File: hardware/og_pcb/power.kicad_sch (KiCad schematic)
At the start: 6 parts, among them J1 USB_C_Receptacle_PowerOnly_6P, U4 BD33FC0FP

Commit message: updated pcb work in progress (incomplete)
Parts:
- removed J1: USB_C_Receptacle_PowerOnly_6P, Connector_USB:USB_C_Receptacle_HRO_TYPE-C-31-M-17, symbol Connector:USB_C_Receptacle_PowerOnly_6P
- removed R8, R9: 5.1k, Resistor_SMD:R_0402_1005Metric, symbol Device:R
- added J3: Barrel_Jack, symbol Connector:Barrel_Jack
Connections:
- net GND: now also J3.2
- net VBUS: now also J3.1
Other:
- note added: "replace usbc power with barrel jack"
- note removed: "(5V Input)"
- note removed: "USB-C Power Input"

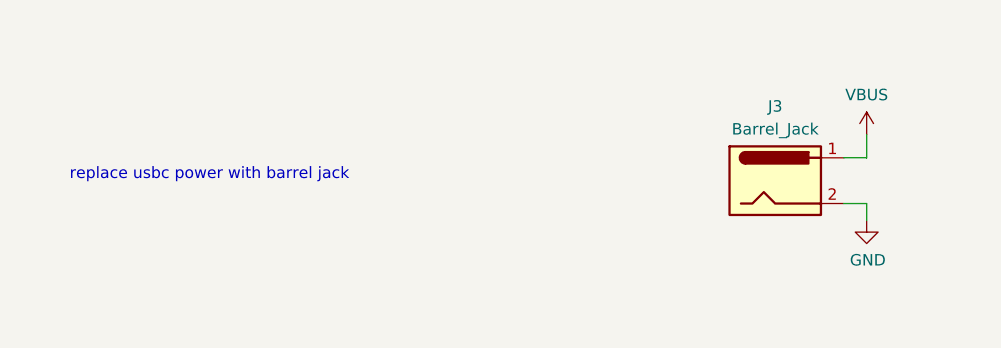
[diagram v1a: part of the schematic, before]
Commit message: updated pcb v2 progress
reimplemented spi microSD, changed power monitor to model with internal shunt resistor, changed power supply from usbc to barrel jack, reconnected vbus to microusb, modified spi and i2c connections (2 i2c connections, 2 spi connections), removed RF module & IMU.

to do:
- find/create footprints for new parts
- verify implementation by reviewing datasheets again
- implement coax connector for analog connection to cosmic watch
- implement gps receiver (must do more research; implement one well-known/documented/used b4)
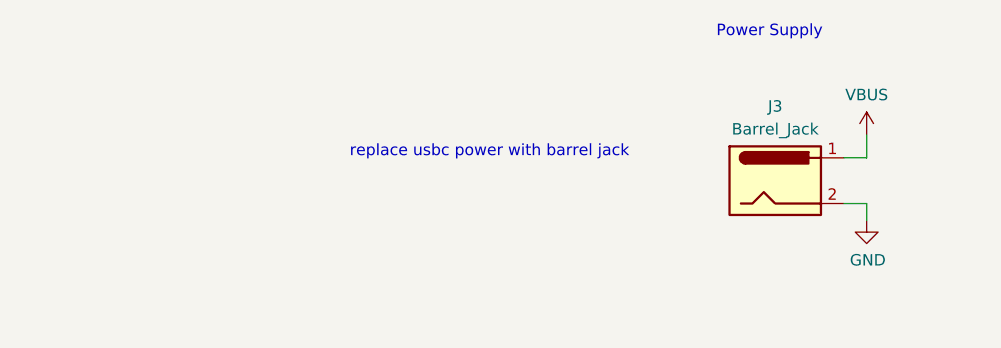
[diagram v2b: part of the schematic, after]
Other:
- note added: "Power Supply"
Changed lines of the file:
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@@
 	(text "replace usbc power with barrel jack"
 		(exclude_from_sim no)
-		(at 49.53 75.565 0)
+		(at 80.645 73.025 0)
 		(effects
 			(font
+				(size 1.27 1.27)
+			)
+		)
+	)
+	(text "Power Supply"
+		(exclude_from_sim no)
+		(at 111.76 59.69 0)
+		(effects
+			(font

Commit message: new preliminary demo pcb
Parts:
- added J5: USB_C_Receptacle_USB2.0_16P, 1my_footprints:microUSB, symbol Connector:USB_C_Receptacle_USB2.0_16P
- added R18, R19: 5.1k, Resistor_SMD:R_0402_1005Metric, symbol Device:R
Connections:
- net GND: now also J5.A1 (GND), J5.A12 (GND), J5.B1 (GND), J5.B12 (GND), J5.S1 (SHIELD), R18.1, R19.2
- net VBUS: now also J5.A4 (VBUS), J5.A9 (VBUS), J5.B4 (VBUS), J5.B9 (VBUS)
- new net: J5.A5 (CC1), R18.2
- new net: J5.B5 (CC2), R19.1
- new net USB_DM: J5.A7 (D-), J5.B7 (D-)
- new net USB_DP: J5.A6 (D+), J5.B6 (D+)
- no-connect marks 0 -> 2
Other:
- note removed: "replace usbc power with barrel jack"

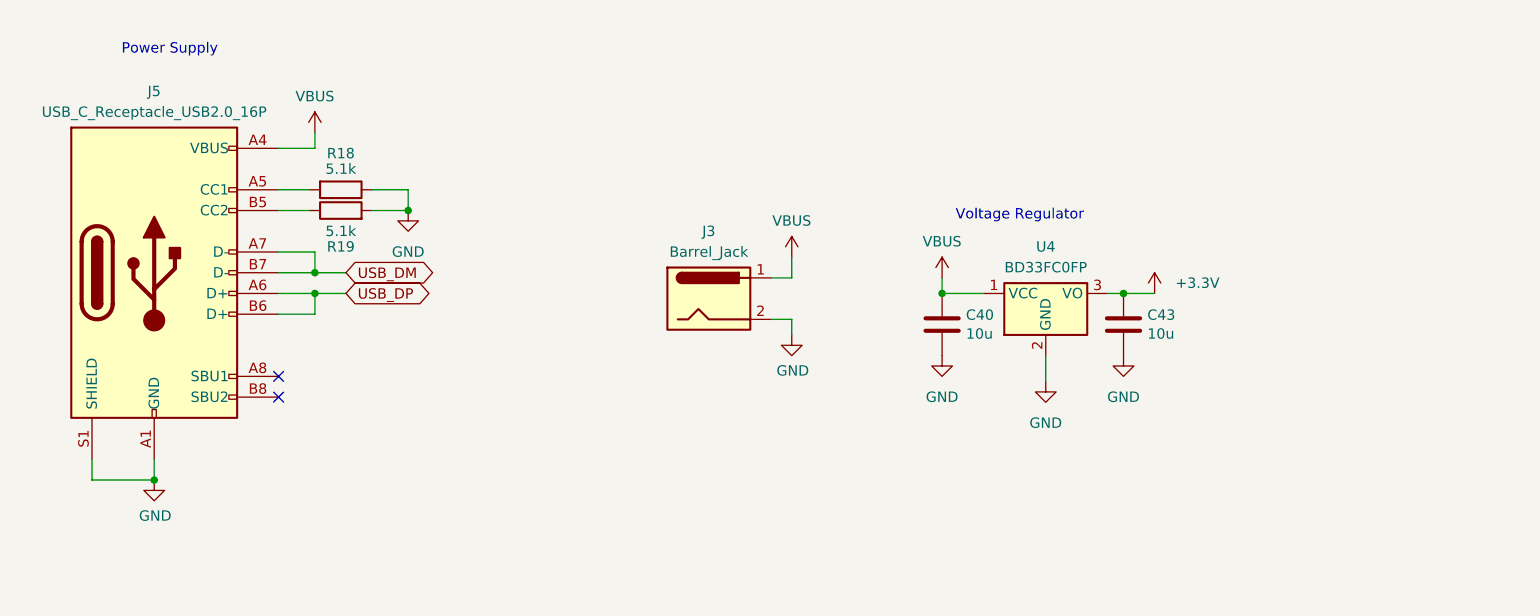
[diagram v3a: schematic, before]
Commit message: updated pcb
added footprints, led, testpoints
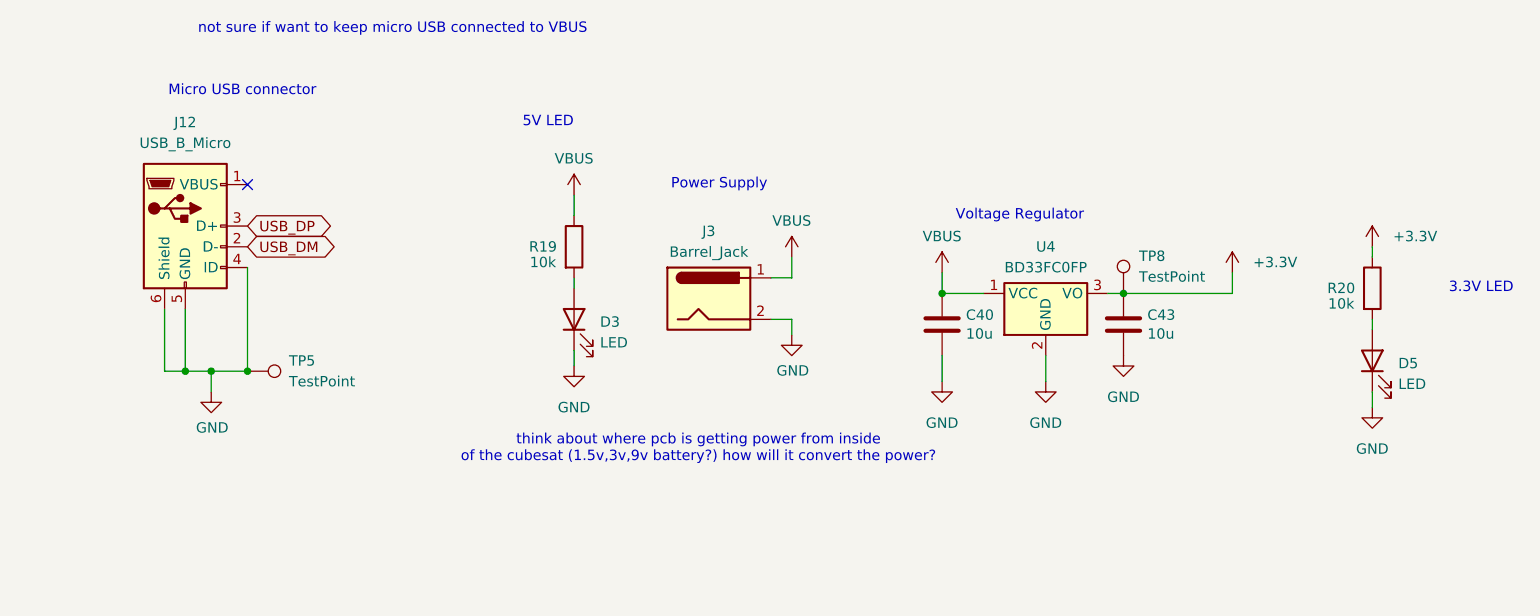
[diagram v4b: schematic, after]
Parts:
- removed J5: USB_C_Receptacle_USB2.0_16P, 1my_footprints:microUSB, symbol Connector:USB_C_Receptacle_USB2.0_16P
- removed R18: 5.1k, Resistor_SMD:R_0402_1005Metric, symbol Device:R
- added D3, D5: LED, LED_SMD:LED_0603_1608Metric, symbol Device:LED
- added J12: USB_B_Micro, 1my_footprints:microUSB, symbol Connector:USB_B_Micro
- added R20: 10k, Resistor_SMD:R_0402_1005Metric, symbol Device:R
- added TP5, TP8: TestPoint, 1my_footprints:TestPoint_Loop_D1.80mm_Drill1.0mm_Beaded, symbol Connector:TestPoint
- J3: footprint (none) -> 1my_footprints:wurthbarreljack694106301002
- R19: value 5.1k -> 10k
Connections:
- net +3.3V: now also R20.1, TP8.1
- net GND: now also D3.1 (K), D5.1 (K), J12.4 (ID), J12.5 (GND), J12.6 (Shield), TP5.1; no longer R19.2
- net USB_DM: now also J12.2 (D-)
- net USB_DP: now also J12.3 (D+)
- net VBUS: now also R19.1
- new net: D3.2 (A), R19.2
- new net: D5.2 (A), R20.2
- no-connect marks 2 -> 1
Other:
- note added: "3.3V LED"
- note added: "5V LED"
- note added: "Micro USB connector"
- note added: "not sure if want to keep micro USB connected to VBUS"
- note added: "think about where pcb is getting power from inside of the cubesat (1.5v,3v,9v battery?) how will it convert the power?"

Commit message: added comments from pragun's review
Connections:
- no-connect marks 1 -> 0
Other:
- note added: "remove barrel jack"
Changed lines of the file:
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@@
+		)
+	)
+	(text "remove barrel jack\n"
+		(exclude_from_sim no)
+		(at 126.365 55.245 0)
+		(effects
+			(font
+				(size 1.27 1.27)
+			)
 		)
 	)
@@
 		(color 0 0 0 0)
 	)
-	(no_connect
-		(at 55.88 62.23)
-	)
 	(wire

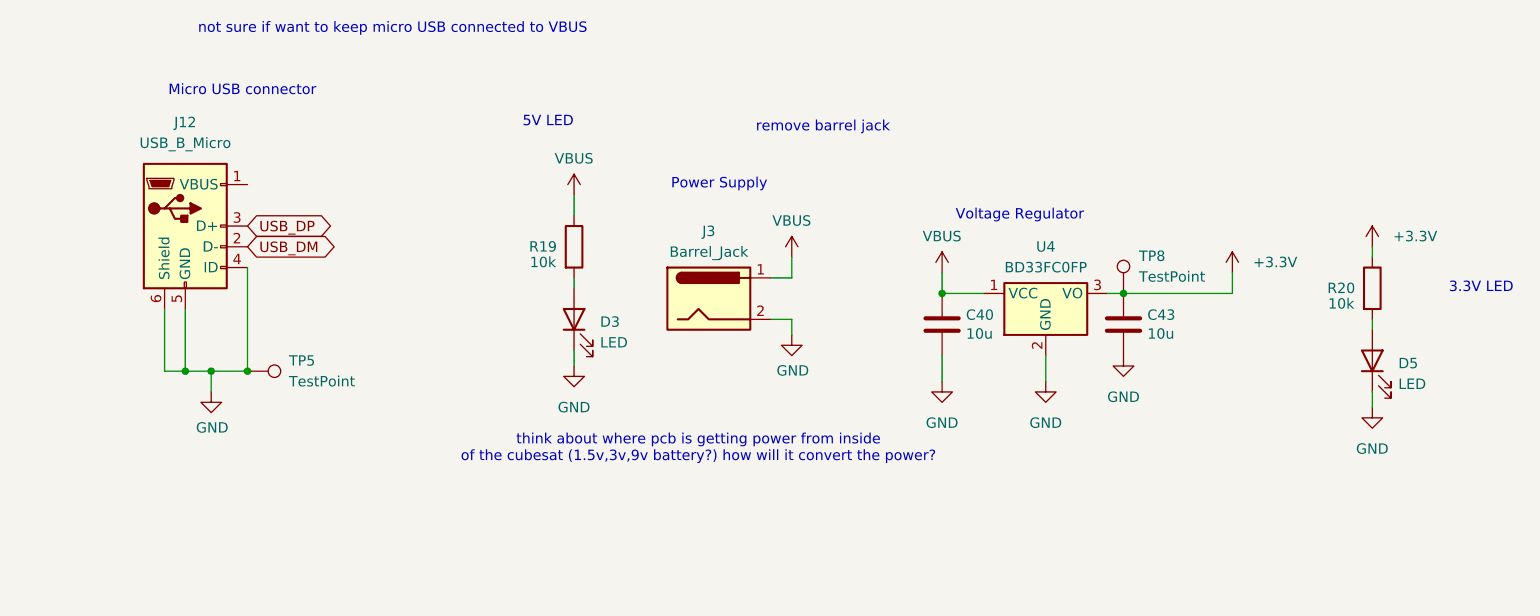
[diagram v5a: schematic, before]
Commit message: implemented pragun's advice
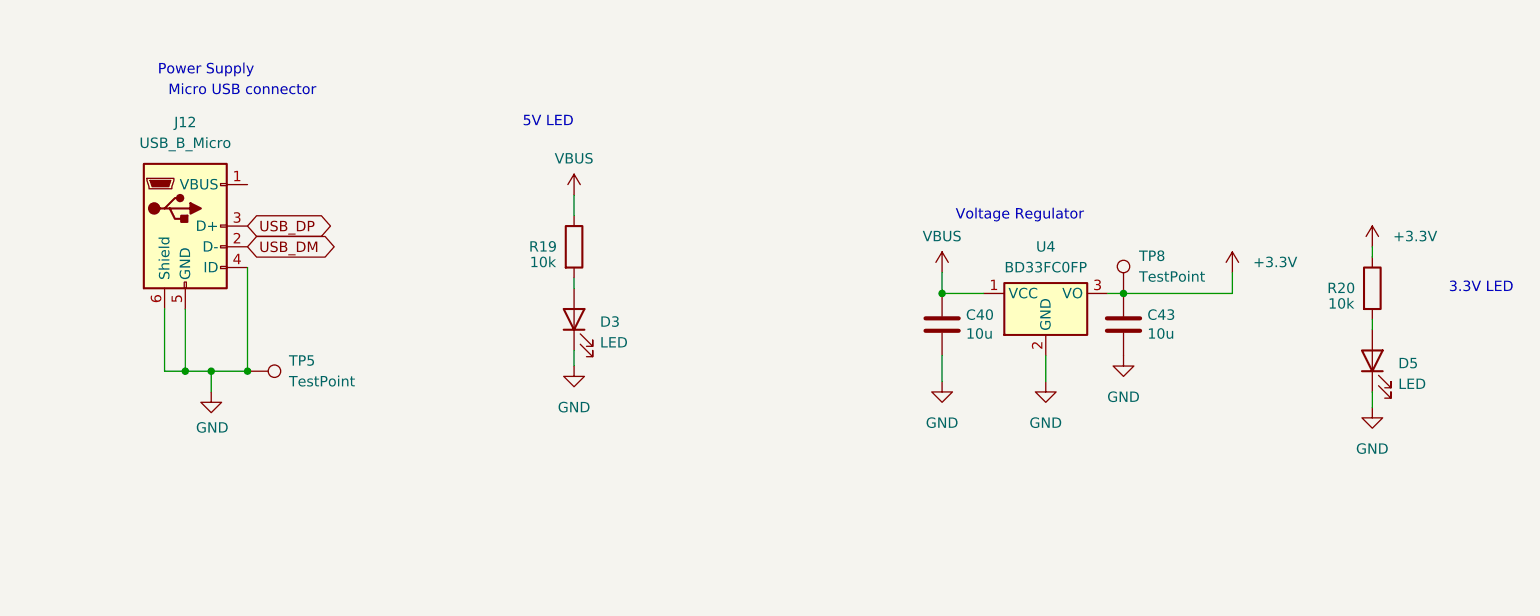
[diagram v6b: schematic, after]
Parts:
- removed J3: Barrel_Jack, 1my_footprints:wurthbarreljack694106301002, symbol Connector:Barrel_Jack
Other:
- note removed: "not sure if want to keep micro USB connected to VBUS"
- note removed: "remove barrel jack"
- note removed: "think about where pcb is getting power from inside of the cubesat (1.5v,3v,9v battery?) how will it convert the power?"
